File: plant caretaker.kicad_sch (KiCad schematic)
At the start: 5 parts, among them U1 UDA1380HN_N2

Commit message: ok
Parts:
- removed R2: R, symbol Device:R
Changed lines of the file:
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@@
-		)
-		(instances
-			(project ""
-				(path "/23b35dcc-615e-4aec-abee-c26cc3d8b906"
-					(reference "R1")
-					(unit 1)
-				)
-			)
-		)
-	)
-	(symbol
-		(lib_id "Device:R")
-		(at 110.49 52.07 0)
-		(unit 1)
-		(exclude_from_sim no)
-		(in_bom yes)
-		(on_board yes)
-		(dnp no)
-		(fields_autoplaced yes)
-		(property "Reference" "R2"
-			(at 113.03 50.7999 0)
-			(effects
-				(font
-					(size 1.27 1.27)
-				)
-				(justify left)
-			)
-		)
-		(property "Value" "R"
-			(at 113.03 53.3399 0)
-			(effects
-				(font
-					(size 1.27 1.27)
-				)
-				(justify left)
-			)
-		)
-		(property "Footprint" ""
-			(at 108.712 52.07 90)
-			(effects
-				(font
-					(size 1.27 1.27)
-				)
-				(hide yes)
-			)
-		)
-		(property "Datasheet" "~"
-			(at 110.49 52.07 0)
-			(effects
-				(font
-					(size 1.27 1.27)
-				)
-				(hide yes)
-			)
-		)
-		(property "Description" "Resistor"
-			(at 110.49 52.07 0)
-			(effects
-				(font
-					(size 1.27 1.27)
-				)
-				(hide yes)
-			)
-		)
-		(pin "1"
-		)
-		(pin "2"
 		)
 		(instances
 			(project "plant caretaker"
 				(path "/23b35dcc-615e-4aec-abee-c26cc3d8b906"
-					(reference "R2")
+					(reference "R1")
 					(unit 1)
 				)
@@
 		)
 		(instances
-			(project ""
+			(project "plant caretaker"
 				(path "/23b35dcc-615e-4aec-abee-c26cc3d8b906"
 					(reference "C1")

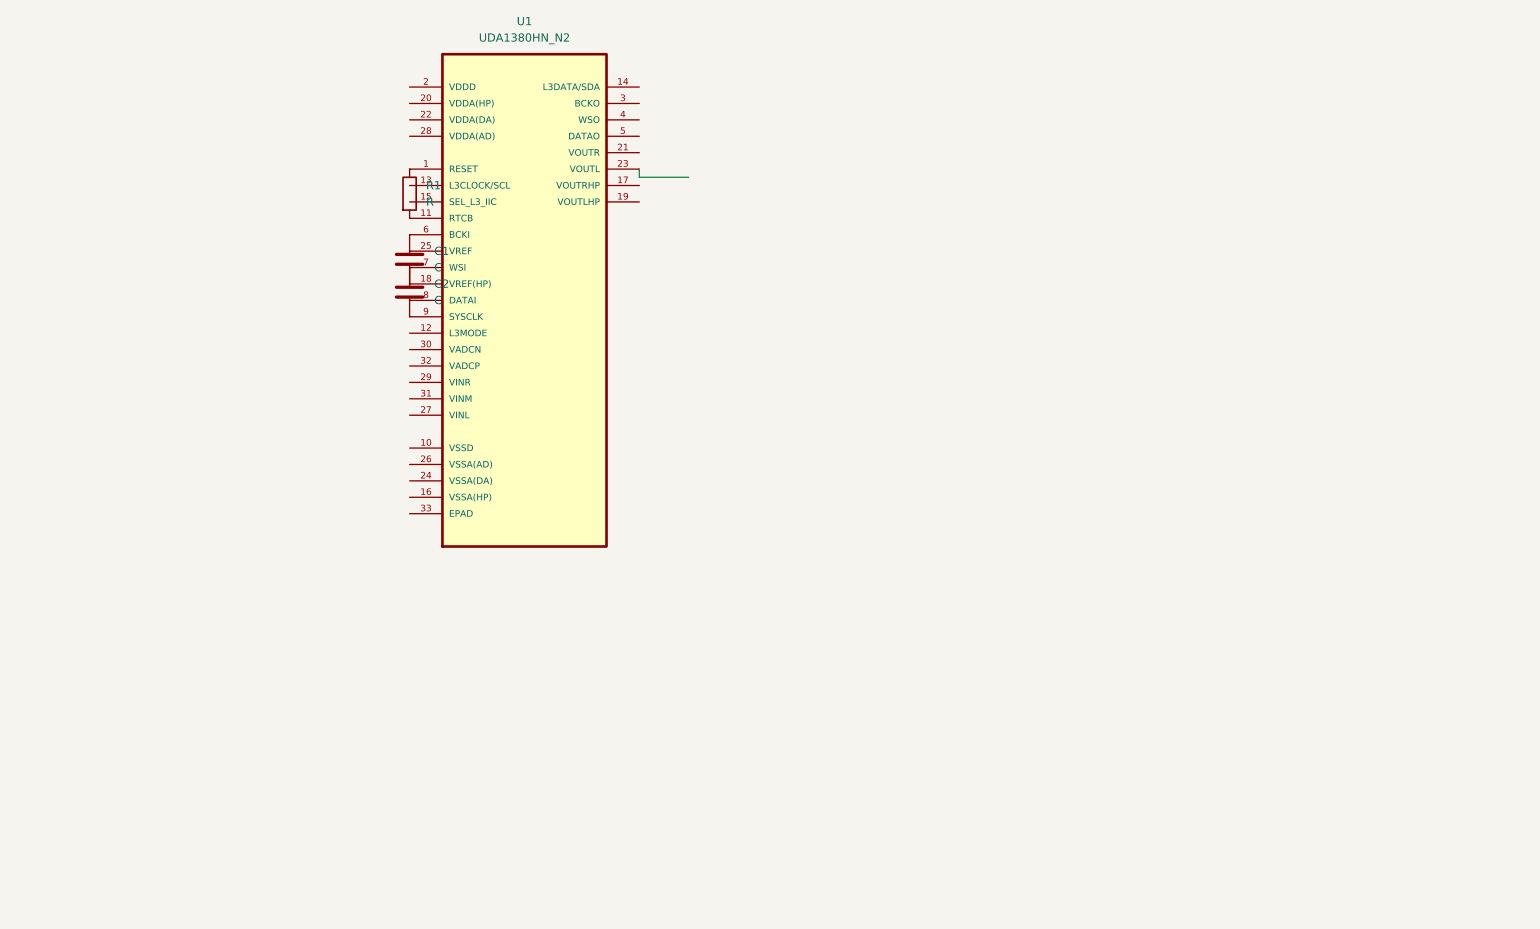
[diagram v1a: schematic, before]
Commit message: Added main components
Added components to the schematic:
-ESP32-C3
-TMP175AIDR
-PAM8403
-LM2576S-ADJ
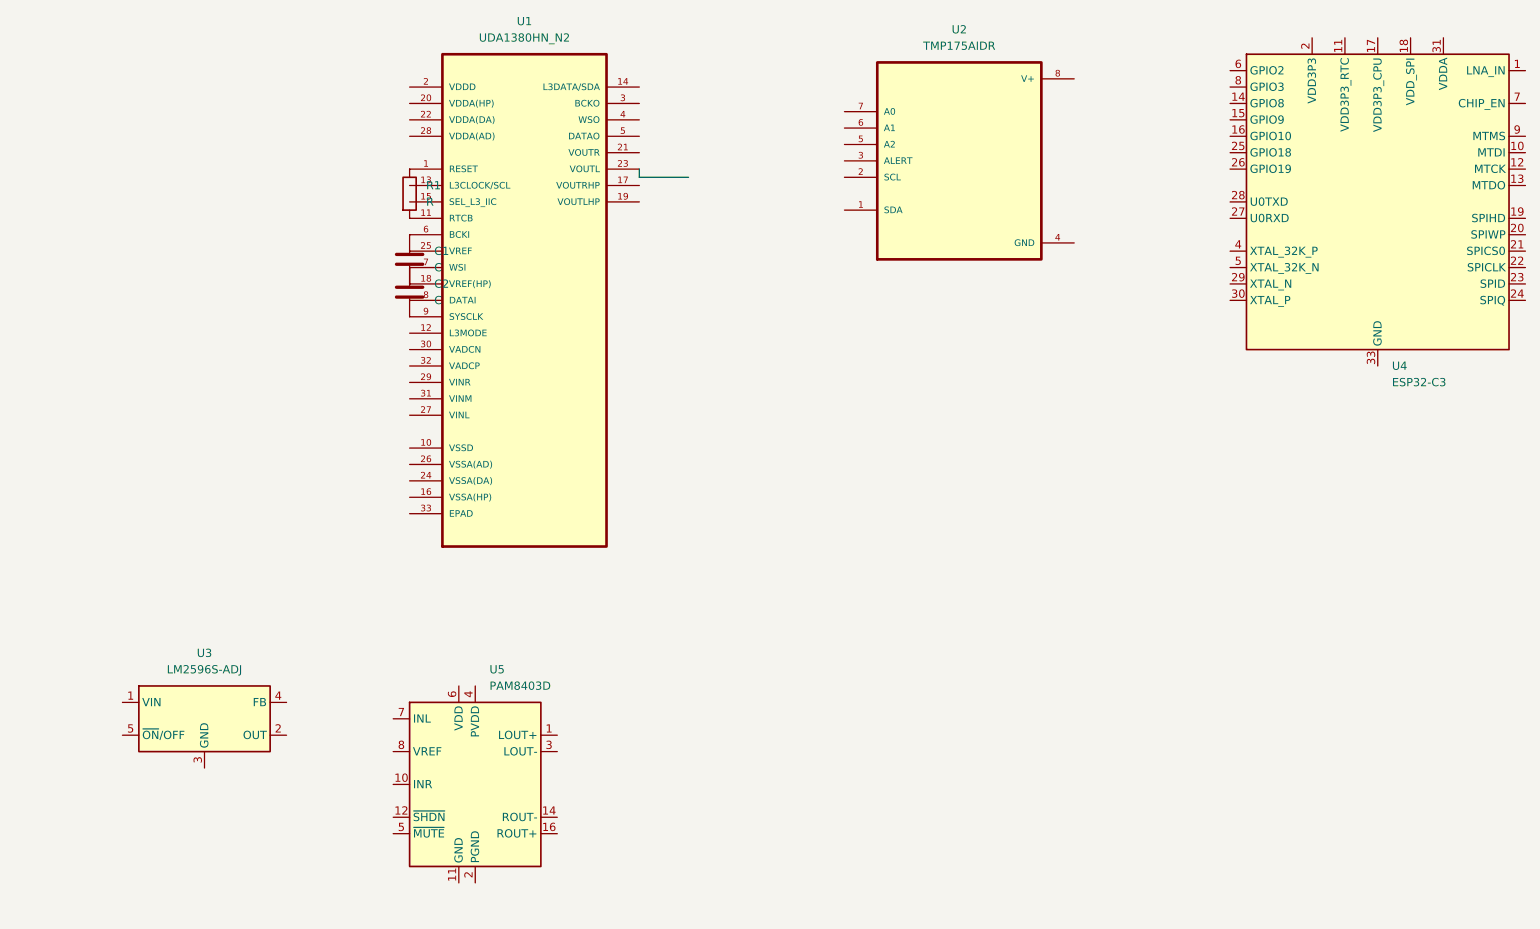
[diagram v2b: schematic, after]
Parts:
- added U2: TMP175AIDR, TMP175AIDR:SOIC127P599X175-8N, symbol TMP175AIDR:TMP175AIDR
- added U3: LM2596S-ADJ, Package_TO_SOT_SMD:TO-263-5_TabPin3, symbol Regulator_Switching:LM2596S-ADJ
- added U4: ESP32-C3, Package_DFN_QFN:QFN-32-1EP_5x5mm_P0.5mm_EP3.7x3.7mm, symbol MCU_Espressif:ESP32-C3
- added U5: PAM8403D, Package_SO:SOP-16_3.9x9.9mm_P1.27mm, symbol Amplifier_Audio:PAM8403D
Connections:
- new net: U4.2 (VDD3P3), U4.3 (VDD3P3)
- new net: U4.31 (VDDA), U4.32 (VDDA)
- new net: U5.13 (PVDD), U5.4 (PVDD)
- new net: U5.15 (PGND), U5.2 (PGND)

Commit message: Added connection schematic
Added connection schematic for Buck Converter
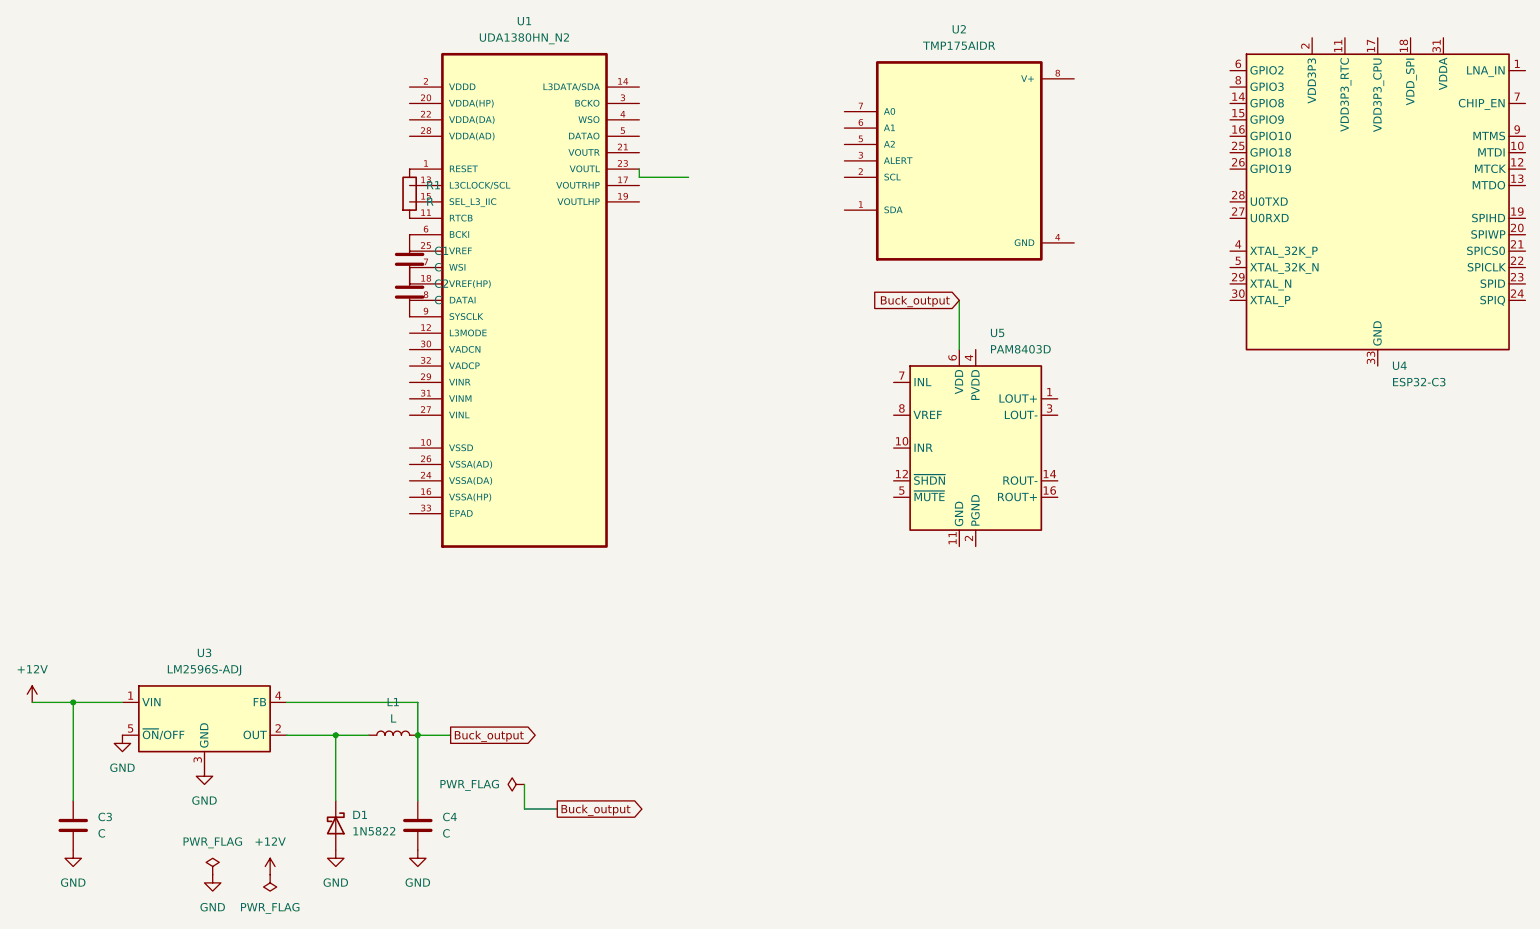
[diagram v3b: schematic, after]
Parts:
- added C3, C4: C, symbol Device:C
- added D1: 1N5822, Diode_THT:D_DO-201AD_P15.24mm_Horizontal, symbol Diode:1N5822
- added L1: L, symbol Device:L
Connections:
- net Buck_output: now reaches U5.6 (VDD)
- net Buck_output: now also U3.4 (FB), C4.1, L1.1
- net +12V: now reaches U3.1 (VIN)
- net +12V: now also C3.1
- net at U3.2 (OUT): now also D1.1 (K), L1.2
- net GND: now reaches U3.3 (GND)
- net GND: now also U3.5 (~{ON}/OFF), C3.2, C4.2, D1.2 (A)
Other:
- moved on the sheet: U5

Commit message: Added hierarchichal pages
Now components are divided into pages so that we can change them without merging with each other's files
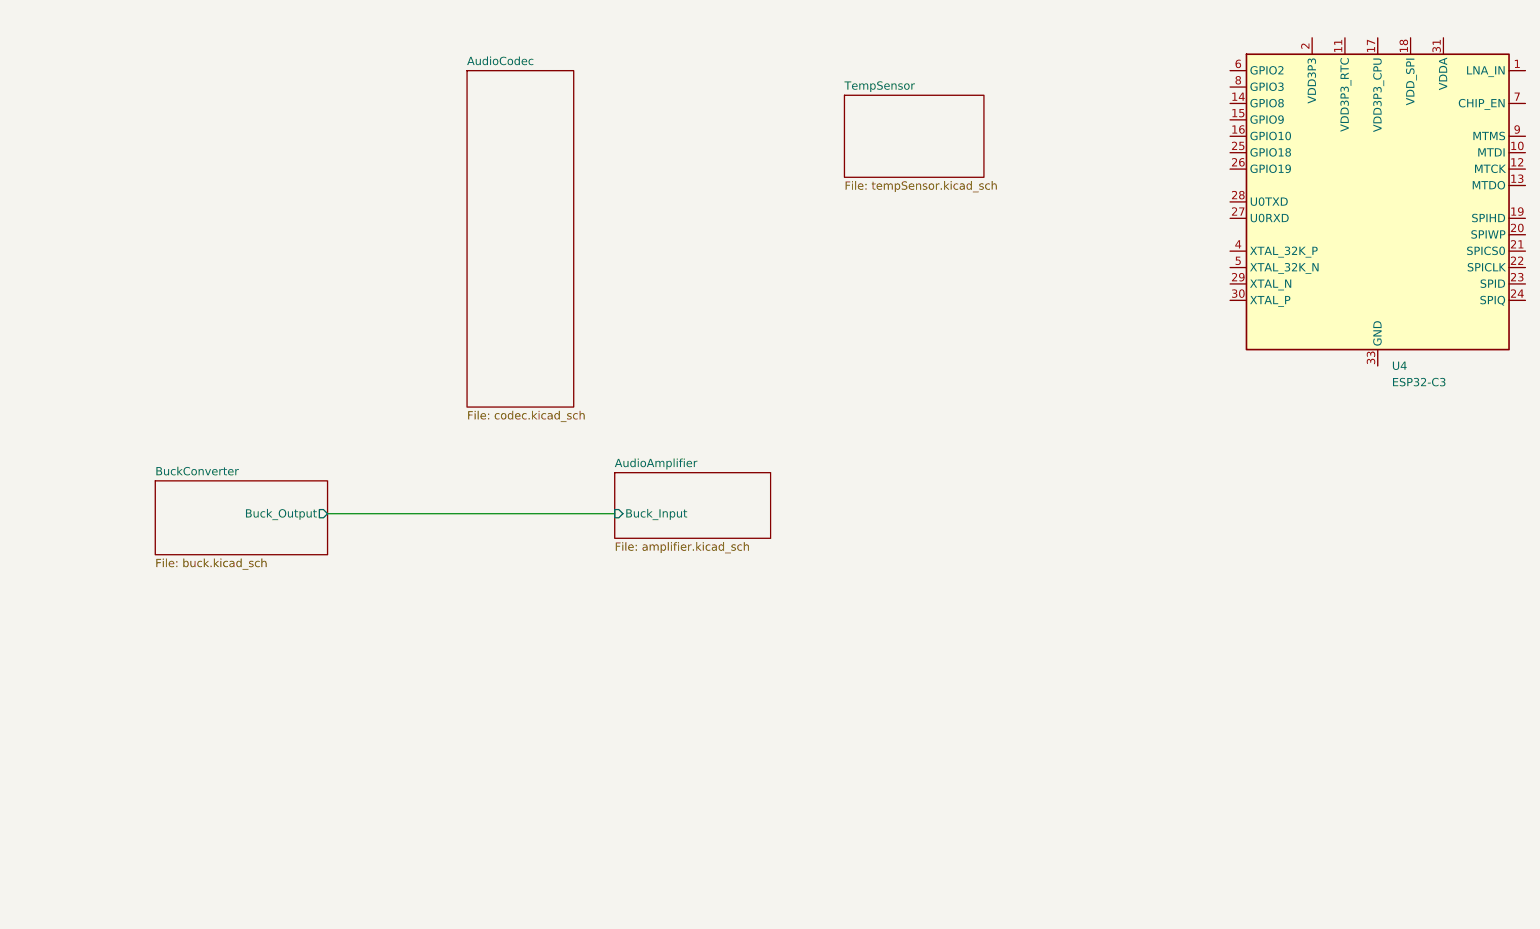
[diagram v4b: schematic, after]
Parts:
- removed C1, C2, C3, C4: C, symbol Device:C
- removed D1: 1N5822, Diode_THT:D_DO-201AD_P15.24mm_Horizontal, symbol Diode:1N5822
- removed L1: L, symbol Device:L
- removed R1: R, symbol Device:R
- removed U1: UDA1380HN_N2, UDA1380HN_N2:QFN50P500X500X100-32N, symbol UDA1380HN_N2:UDA1380HN_N2
- removed U2: TMP175AIDR, TMP175AIDR:SOIC127P599X175-8N, symbol TMP175AIDR:TMP175AIDR
- removed U3: LM2596S-ADJ, Package_TO_SOT_SMD:TO-263-5_TabPin3, symbol Regulator_Switching:LM2596S-ADJ
- removed U5: PAM8403D, Package_SO:SOP-16_3.9x9.9mm_P1.27mm, symbol Amplifier_Audio:PAM8403D
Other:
- added sheet AudioAmplifier (amplifier.kicad_sch)
- added sheet AudioCodec (codec.kicad_sch)
- added sheet BuckConverter (buck.kicad_sch)
- added sheet TempSensor (tempSensor.kicad_sch)

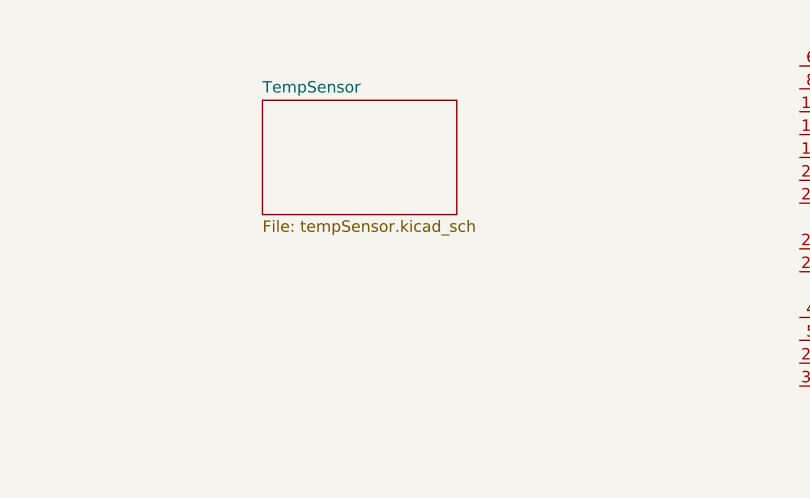
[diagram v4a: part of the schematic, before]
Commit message: Added pins to temp sensor
Hierarchy input/output for the sensor schematic and the root
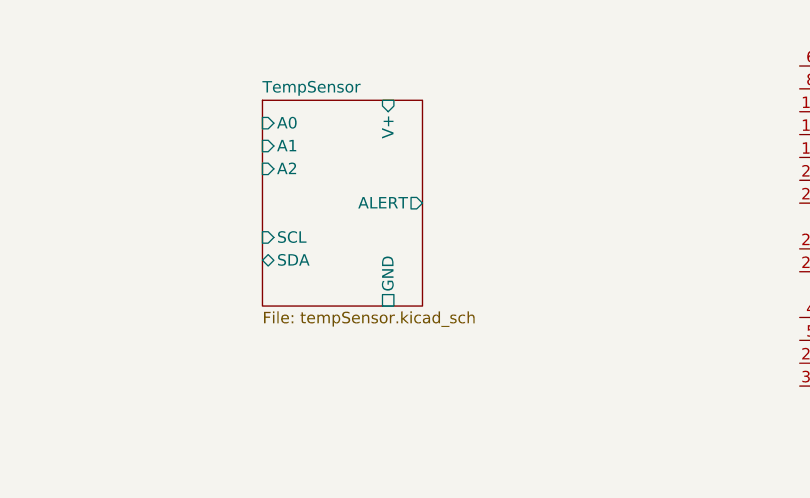
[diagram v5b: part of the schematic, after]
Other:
- sheet TempSensor ports: added A0, A1, A2, ALERT, GND, SCL, SDA, V+; removed none
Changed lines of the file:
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@@
 	(sheet
 		(at 142.24 39.37)
-		(size 21.59 12.7)
+		(size 17.78 22.86)
 		(fields_autoplaced yes)
 		(stroke
@@
 		)
 		(property "Sheetfile" "tempSensor.kicad_sch"
-			(at 142.24 52.6546 0)
+			(at 142.24 62.8146 0)
 			(effects
 				(font
@@
 			)
 		)
+		(pin "A1" input
+			(at 142.24 44.45 180)
+			(effects
+				(font
+					(size 1.27 1.27)
+				)
+				(justify left)
+			)
+		)
+		(pin "A0" input
+			(at 142.24 41.91 180)
+			(effects
+				(font
+					(size 1.27 1.27)
+				)
+				(justify left)
+			)
+		)
+		(pin "SCL" input
+			(at 142.24 54.61 180)
+			(effects
+				(font
+					(size 1.27 1.27)
+				)
+				(justify left)
+			)
+		)
+		(pin "A2" input
+			(at 142.24 46.99 180)
+			(effects
+				(font
+					(size 1.27 1.27)
+				)
+				(justify left)
+			)
+		)
+		(pin "ALERT" output
+			(at 160.02 50.8 0)
+			(effects
+				(font
+					(size 1.27 1.27)
+				)
+				(justify right)
+			)
+		)
+		(pin "SDA" bidirectional
+			(at 142.24 57.15 180)
+			(effects
+				(font
+					(size 1.27 1.27)
+				)
+				(justify left)
+			)
+		)
+		(pin "V+" input
+			(at 156.21 39.37 90)
+			(effects
+				(font
+					(size 1.27 1.27)
+				)
+				(justify right)
+			)
+		)
+		(pin "GND" passive
+			(at 156.21 62.23 270)
+			(effects
+				(font
+					(size 1.27 1.27)
+				)
+				(justify left)
+			)
+		)

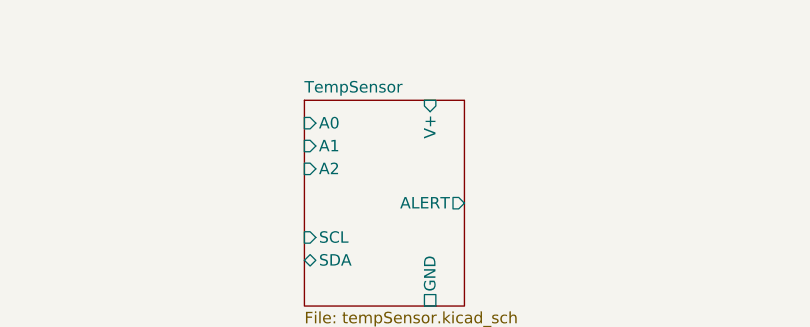
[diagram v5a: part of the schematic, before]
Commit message: Added layout components and comment
Bypass capacitor and pullup resistors according to datasheet
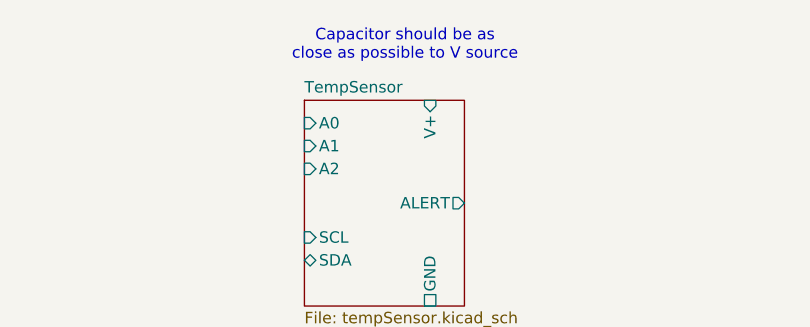
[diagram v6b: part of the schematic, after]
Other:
- note added: "Capacitor should be as close as possible to V source"
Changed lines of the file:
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@@
+		)
+	)
+	(text "Capacitor should be as \nclose as possible to V source\n"
+		(exclude_from_sim no)
+		(at 153.416 33.274 0)
+		(effects
+			(font
+				(size 1.27 1.27)
+			)
 		)
 	)

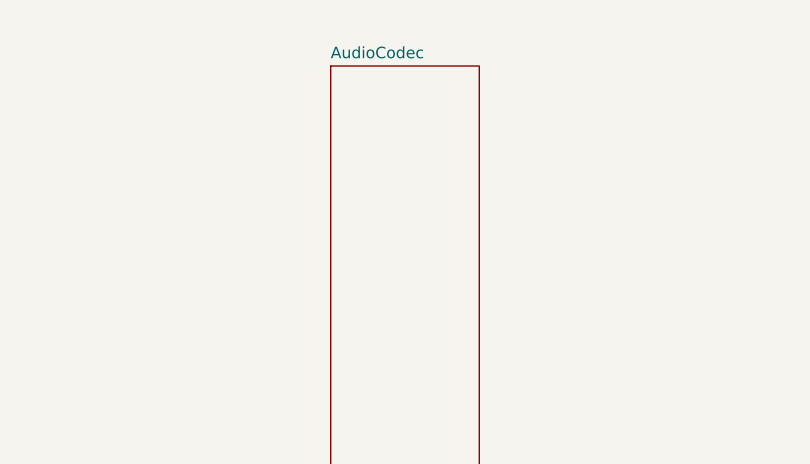
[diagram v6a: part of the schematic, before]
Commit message: Organized codec and imported pins
Also changed color of microchips in main
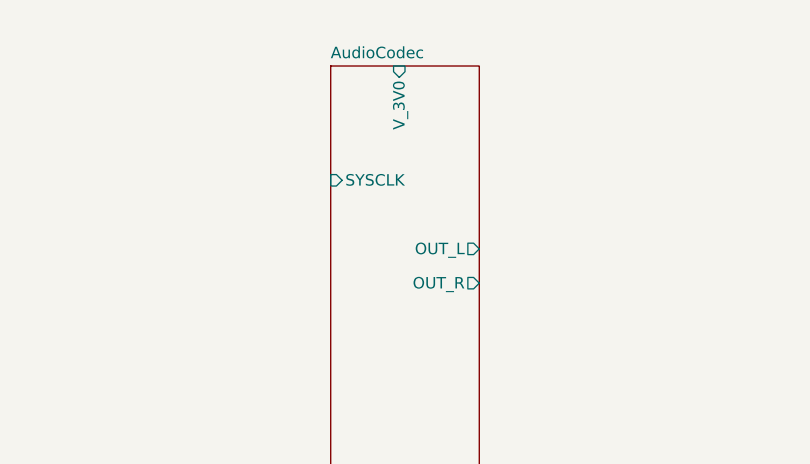
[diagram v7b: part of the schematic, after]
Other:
- sheet AudioCodec ports: added OUT_L, OUT_R, SYSCLK, V_3V0; removed none
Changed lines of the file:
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@@
 		)
 		(fill
-			(color 255 249 178 1.0000)
+			(color 255 255 207 1.0000)
 		)
 		(property "Sheetname" "AudioCodec"
@@
 			)
 		)
+		(pin "V_3V0" input
+			(at 91.44 35.56 90)
+			(effects
+				(font
+					(size 1.27 1.27)
+				)
+				(justify right)
+			)
+		)
+		(pin "SYSCLK" input
+			(at 83.82 48.26 180)
+			(effects
+				(font
+					(size 1.27 1.27)
+				)
+				(justify left)
+			)
+		)
+		(pin "OUT_L" output
+			(at 100.33 55.88 0)
+			(effects
+				(font
+					(size 1.27 1.27)
+				)
+				(justify right)
+			)
+		)
+		(pin "OUT_R" output
+			(at 100.33 59.69 0)
+			(effects
+				(font
+					(size 1.27 1.27)
+				)
+				(justify right)
+			)
+		)
 		(instances
 			(project "plant caretaker"
@@
 		)
 		(fill
-			(color 255 252 216 1.0000)
+			(color 255 255 207 1.0000)
 		)
 		(property "Sheetname" "BuckConverter"
@@
 		)
 		(fill
-			(color 255 251 218 1.0000)
+			(color 255 255 207 1.0000)
 		)
 		(property "Sheetname" "AudioAmplifier"
@@
 		)
 		(fill
-			(color 255 253 203 1.0000)
+			(color 255 255 207 1.0000)
 		)
 		(property "Sheetname" "TempSensor"
